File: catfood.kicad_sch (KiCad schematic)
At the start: 0 parts

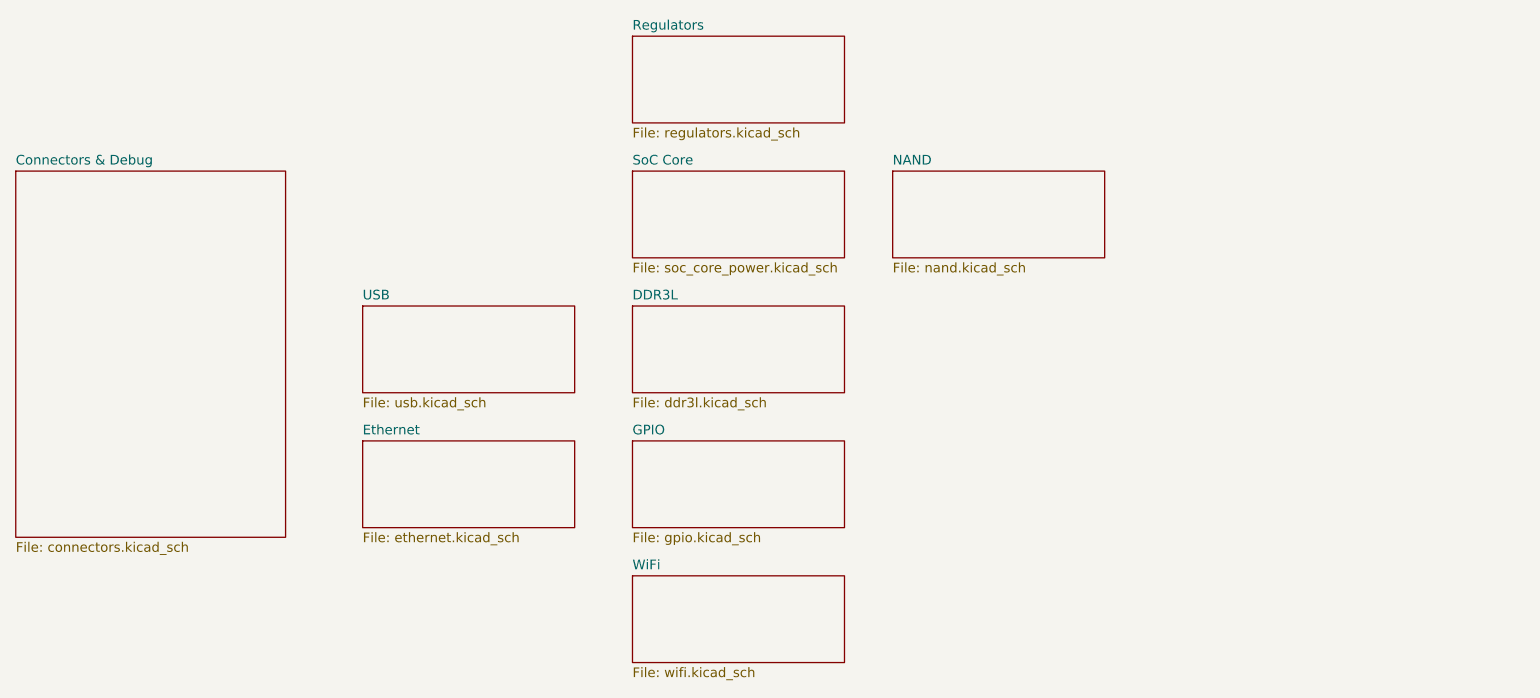
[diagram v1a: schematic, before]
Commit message: Core power; clock/ctrl
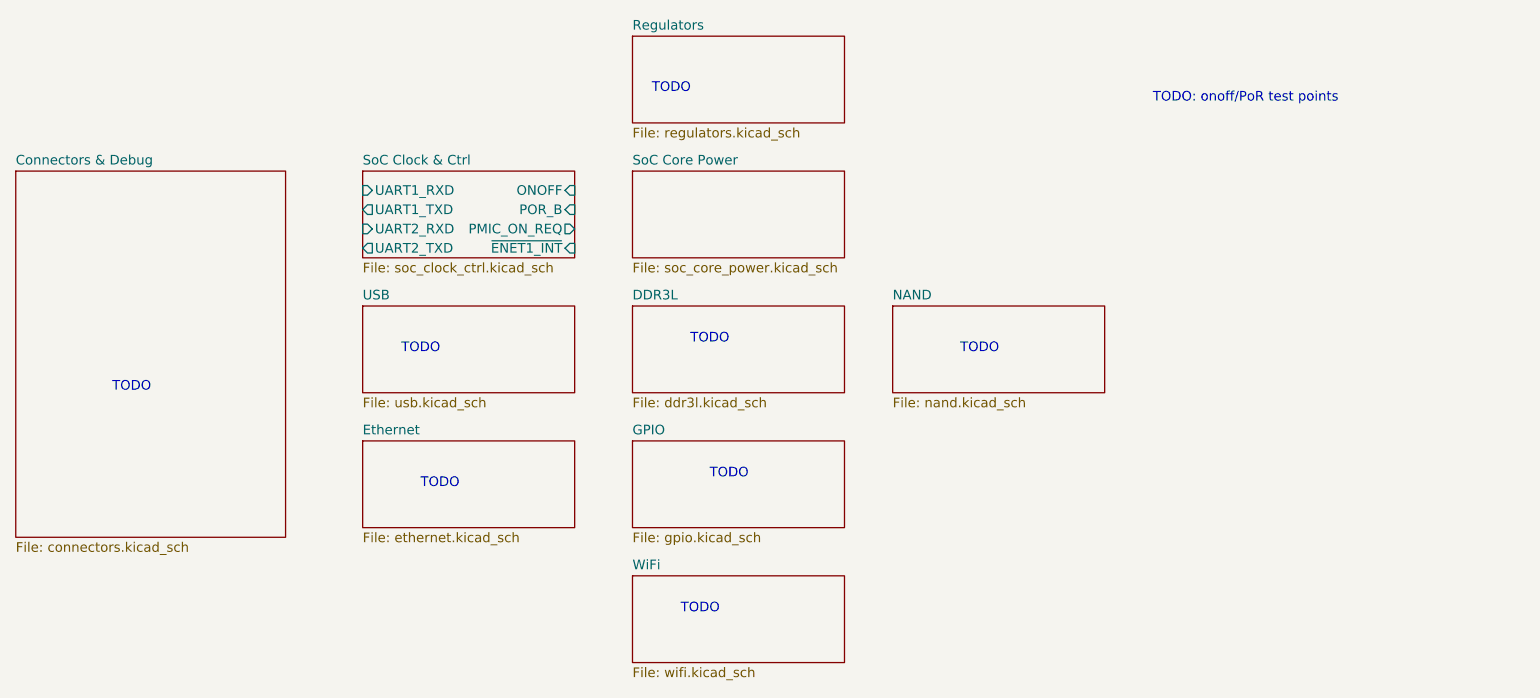
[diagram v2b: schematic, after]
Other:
- sheet SoC Core renamed SoC Core Power
- added sheet SoC Clock & Ctrl (soc_clock_ctrl.kicad_sch)
- note added: "TODO"
- note added: "TODO: onoff/PoR test points"

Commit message: Regulators
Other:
- sheet Regulators ports: added PMIC_ON_REQ; removed none
- note added: "TODO: onoff/PoR/pmic_on_req test points"
- note removed: "TODO: onoff/PoR test points"

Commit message: Remove WiFi
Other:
- removed sheet WiFi
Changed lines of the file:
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@@
-    (effects (font (size 1.27 1.27)) (justify left bottom))
-  )
-  (text "TODO" (at 109.22 100.33 0)
     (effects (font (size 1.27 1.27)) (justify left bottom))
   )
@@
     )
     (property "Sheet file" "nand.kicad_sch" (id 1) (at 137.16 71.7046 0)
-      (effects (font (size 1.27 1.27)) (justify left top))
-    )
-  )
-  (sheet (at 102.87 95.25) (size 27.94 11.43) (fields_autoplaced)
-    (stroke (width 0.1524) (type solid) (color 0 0 0 0))
-    (fill (color 0 0 0 0.0000))
-    (property "Sheet name" "WiFi" (id 0) (at 102.87 94.5384 0)
-      (effects (font (size 1.27 1.27)) (justify left bottom))
-    )
-    (property "Sheet file" "wifi.kicad_sch" (id 1) (at 102.87 107.2646 0)
       (effects (font (size 1.27 1.27)) (justify left top))
     )
@@
     (path "/070bf4c0-20e4-46ea-85ff-83bf5a0585a3" (page "6"))
     (path "/a3321ecb-7e45-4b88-8ac6-91bd0372968a" (page "7"))
-    (path "/0bb953a9-9c38-4653-8755-72b71e851211" (page "8"))
     (path "/1f7c86fd-838a-4fbd-9ad6-fe73640b467f" (page "9"))
     (path "/9e9d365b-50b6-4e60-9e2a-c60cbf357141" (page "10"))
@@
       (reference "U1") (unit 8) (value "MCIMX6Y2DVM09AB") (footprint "")
     )
-    (path "/0bb953a9-9c38-4653-8755-72b71e851211/3c03845e-6e0c-41be-9bcf-762be44e9517"
-      (reference "U1") (unit 9) (value "MCIMX6Y2DVM09AB") (footprint "")
-    )
     (path "/070bf4c0-20e4-46ea-85ff-83bf5a0585a3/578b9c34-21ad-4bde-a728-85eb81977179"
       (reference "U1") (unit 10) (value "MCIMX6Y2DVM09AB") (footprint "")
@@
       (reference "U?") (unit 2) (value "MCIMX6Y2DVM09AB") (footprint "")
     )
+    (path "/1f7c86fd-838a-4fbd-9ad6-fe73640b467f/1e4aacdc-9178-46b1-831c-e66ca079f1f1"
+      (reference "U?") (unit 9) (value "MCIMX6Y2DVM09AB") (footprint "")
+    )
     (path "/f3ebd76f-b12f-4b33-bd17-edae6bffa200/1775a2ca-2f99-43fb-9cc5-88fd1d54cd77"

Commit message: Add LAN8700 symbol
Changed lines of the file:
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@@
     (effects (font (size 1.27 1.27)) (justify left bottom))
   )
-  (text "TODO: onoff/PoR/pmic_on_req test points" (at 171.45 33.02 0)
+  (text "TODO: onoff/PoR/pmic_on_req test points" (at 50.8 33.02 0)
     (effects (font (size 1.27 1.27)) (justify left bottom))
   )
@@
       (reference "#PWR?") (unit 1) (value "GND") (footprint "")
     )
+    (path "/a3321ecb-7e45-4b88-8ac6-91bd0372968a/9798fbb5-87a6-455e-8929-32fa31c7860f"
+      (reference "#PWR?") (unit 1) (value "GND") (footprint "")
+    )
     (path "/e1490e46-0057-4bf0-bc0e-723ccd3e21a2/9a9e918f-0ea8-4f84-95f1-c8607d7cc163"
       (reference "#PWR?") (unit 1) (value "GND") (footprint "")
@@
       (reference "#PWR?") (unit 1) (value "VDD_3V3") (footprint "")
     )
+    (path "/a3321ecb-7e45-4b88-8ac6-91bd0372968a/c2f216b5-abaf-4b8c-9f5a-f3b782b7cfcd"
+      (reference "#PWR?") (unit 1) (value "VDD_3V3") (footprint "")
+    )
     (path "/f3ebd76f-b12f-4b33-bd17-edae6bffa200/dcfe82b4-728e-47e9-b293-74162304364f"
       (reference "#PWR?") (unit 1) (value "GND") (footprint "")
@@
       (reference "C?") (unit 1) (value "10uF 0805") (footprint "")
     )
+    (path "/a3321ecb-7e45-4b88-8ac6-91bd0372968a/3682212d-b684-4e0b-9460-4a3d9e57e1b1"
+      (reference "C?") (unit 1) (value "0.22uF 0402") (footprint "")
+    )
     (path "/e1490e46-0057-4bf0-bc0e-723ccd3e21a2/616a633c-9b9e-4f13-b951-4d3018cdc580"
       (reference "C?") (unit 1) (value "DNI 0402") (footprint "")
@@
       (reference "U?") (unit 1) (value "LMR10510XMF") (footprint "Package_TO_SOT_SMD:SOT-23-5")
     )
+    (path "/a3321ecb-7e45-4b88-8ac6-91bd0372968a/bdbfdce4-d165-490f-9bbb-5d1a15aea6a5"
+      (reference "U?") (unit 1) (value "LAN8700C-AEZG") (footprint "")
+    )
     (path "/e1490e46-0057-4bf0-bc0e-723ccd3e21a2/be8ec1dd-a9ac-4bea-96db-c07b6eb52f80"

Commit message: Ethernet schematic
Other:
- sheet Ethernet ports: added ENET_MDC, ENET_MDIO, ~{ENET1_INT}, ~{ENET1_RST}; removed none
